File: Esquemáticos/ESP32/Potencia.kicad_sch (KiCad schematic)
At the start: 11 parts, among them J3 Barrel_Jack, SW1 SW_DIP_x01, U5 AMS1117-5.0, U6 AMS1117-3.3

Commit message: Eliminando el error de autosave
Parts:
- added D1: Led_ON, LED_SMD:LED_1206_3216Metric, symbol LED:IR26-21C_L110_TR8
- SW1: footprint (none) -> Button_Switch_SMD:SW_DIP_SPSTx01_Slide_6.7x4.1mm_W6.73mm_P2.54mm_LowProfile_JPin
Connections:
- net 3.3V: now also D1.2 (A)
- net GND: now also D1.1 (K)
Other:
- note added: "Led de encendido"
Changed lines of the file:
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@@
+    (stroke (width 0) (type default) (color 0 0 0 0))
+  )
+  (polyline (pts (xy 238.76 123.19) (xy 238.76 152.4))
     (stroke (width 0) (type default) (color 0 0 0 0))
   )
@@
     (stroke (width 0) (type default) (color 0 0 0 0))
   )
+  (polyline (pts (xy 257.81 152.4) (xy 257.81 123.19))
+    (stroke (width 0) (type default) (color 0 0 0 0))
+  )
   (wire (pts (xy 163.83 138.43) (xy 163.83 143.51))
     (stroke (width 0) (type default) (color 0 0 0 0))
@@
     (stroke (width 0) (type default) (color 0 0 0 0))
   )
+  (polyline (pts (xy 238.76 123.19) (xy 257.81 123.19))
+    (stroke (width 0) (type default) (color 0 0 0 0))
+  )
+  (wire (pts (xy 245.11 139.7) (xy 245.11 142.24))
+    (stroke (width 0) (type default) (color 0 0 0 0))
+  )
   (wire (pts (xy 207.01 91.44) (xy 207.01 88.9))
     (stroke (width 0) (type default) (color 0 0 0 0))
@@
     (stroke (width 0) (type default) (color 0 0 0 0))
   )
+  (wire (pts (xy 245.11 130.81) (xy 245.11 132.08))
+    (stroke (width 0) (type default) (color 0 0 0 0))
+  )
   (wire (pts (xy 163.83 120.65) (xy 163.83 128.27))
     (stroke (width 0) (type default) (color 0 0 0 0))
@@
     (stroke (width 0) (type default) (color 0 0 0 0))
   )
+  (polyline (pts (xy 238.76 152.4) (xy 257.81 152.4))
+    (stroke (width 0) (type default) (color 0 0 0 0))
+  )
   (wire (pts (xy 160.02 88.9) (xy 160.02 91.44))
     (stroke (width 0) (type default) (color 0 0 0 0))
@@
   )
   (text "Entrada de alimentación de 12V mediante un Jack " (at 76.2 123.19 0)
+    (effects (font (size 1.27 1.27)) (justify left bottom))
+  )
+  (text "Led de encendido\n" (at 238.76 156.21 0)
     (effects (font (size 1.27 1.27)) (justify left bottom))
   )
@@
   )
   (hierarchical_label "3.3V" (shape input) (at 207.01 123.19 90)
+    (effects (font (size 1.27 1.27)) (justify left))
+  )
+  (hierarchical_label "3.3V" (shape input) (at 245.11 130.81 90)
     (effects (font (size 1.27 1.27)) (justify left))
   )
@@
     (pin "1")
   )
+  (symbol (lib_id "LED:IR26-21C_L110_TR8") (at 245.11 135.89 90) (unit 1)
+    (in_bom yes) (on_board yes) (fields_autoplaced)
+    (property "Reference" "D1" (id 0) (at 248.92 136.2074 90)
+      (effects (font (size 1.27 1.27)) (justify right))
+    )
+    (property "Value" "Led_ON" (id 1) (at 248.92 138.7474 90)
+      (effects (font (size 1.27 1.27)) (justify right))
+    )
+    (property "Footprint" "LED_SMD:LED_1206_3216Metric" (id 2) (at 240.03 135.89 0)
+      (effects (font (size 1.27 1.27)) hide)
+    )
+    (property "Datasheet" "http://www.everlight.com/file/ProductFile/IR26-21C-L110-TR8.pdf" (id 3) (at 245.11 135.89 0)
+      (effects (font (size 1.27 1.27)) hide)
+    )
+    (pin "1")
+    (pin "2")
+  )
   (symbol (lib_id "Device:C_Polarized_US") (at 163.83 134.62 0) (unit 1)
     (in_bom yes) (on_board yes)
@@
     (pin "1")
   )
+  (symbol (lib_id "power:GND") (at 245.11 142.24 0) (unit 1)
+    (in_bom yes) (on_board yes) (fields_autoplaced)
+    (property "Reference" "#PWR0101" (id 0) (at 245.11 148.59 0)
+      (effects (font (size 1.27 1.27)) hide)
+    )
+    (property "Value" "GND" (id 1) (at 245.11 147.32 0))
+    (property "Footprint" "" (id 2) (at 245.11 142.24 0)
+      (effects (font (size 1.27 1.27)) hide)
+    )
+    (property "Datasheet" "" (id 3) (at 245.11 142.24 0)
+      (effects (font (size 1.27 1.27)) hide)
+    )
+    (pin "1")
+  )
   (symbol (lib_id "power:GND") (at 113.03 107.95 0) (unit 1)
     (in_bom yes) (on_board yes) (fields_autoplaced)
@@
     (property "Reference" "SW1" (id 0) (at 88.9 81.28 0))
     (property "Value" "SW_DIP_x01" (id 1) (at 88.9 83.82 0))
-    (property "Footprint" "" (id 2) (at 88.9 88.9 0)
-      (effects (font (size 1.27 1.27)) hide)
-    )
+    (property "Footprint" "Button_Switch_SMD:SW_DIP_SPSTx01_Slide_6.7x4.1mm_W6.73mm_P2.54mm_LowProfile_JPin" (id 2) (at 88.9 88.9 0)
+      (effects (font (size 1.27 1.27)) hide)
+    )

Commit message: Etiquetas globales para alimentación añadidas
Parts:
- C11: footprint (none) -> Capacitor_SMD:C_0201_0603Metric_Pad0.64x0.40mm_HandSolder
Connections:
- net Earth is gone; now on net GND: J3.2
- net 12V renamed +12V
- net 3.3V renamed +3.3V
- net 5V renamed +5V
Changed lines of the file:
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@@
     (effects (font (size 1.27 1.27)) (justify left bottom))
-  )
-  (hierarchical_label "3.3V" (shape input) (at 207.01 123.19 90)
-    (effects (font (size 1.27 1.27)) (justify left))
-  )
-  (hierarchical_label "3.3V" (shape input) (at 245.11 130.81 90)
-    (effects (font (size 1.27 1.27)) (justify left))
-  )
-  (hierarchical_label "12V" (shape input) (at 128.27 82.55 90)
-    (effects (font (size 1.27 1.27)) (justify left))
-  )
-  (hierarchical_label "5V" (shape input) (at 207.01 83.82 90)
-    (effects (font (size 1.27 1.27)) (justify left))
   )
   (symbol (lib_id "Regulator_Linear:AMS1117-5.0") (at 182.88 88.9 0) (unit 1)
@@
     (pin "1")
   )
+  (symbol (lib_id "power:+12V") (at 128.27 82.55 0) (unit 1)
+    (in_bom yes) (on_board yes) (fields_autoplaced)
+    (property "Reference" "#PWR021" (id 0) (at 128.27 86.36 0)
+      (effects (font (size 1.27 1.27)) hide)
+    )
+    (property "Value" "+12V" (id 1) (at 128.27 77.47 0))
+    (property "Footprint" "" (id 2) (at 128.27 82.55 0)
+      (effects (font (size 1.27 1.27)) hide)
+    )
+    (property "Datasheet" "" (id 3) (at 128.27 82.55 0)
+      (effects (font (size 1.27 1.27)) hide)
+    )
+    (pin "1")
+  )
   (symbol (lib_id "LED:IR26-21C_L110_TR8") (at 245.11 135.89 90) (unit 1)
     (in_bom yes) (on_board yes) (fields_autoplaced)
@@
     )
     (property "Datasheet" "" (id 3) (at 182.88 105.41 0)
+      (effects (font (size 1.27 1.27)) hide)
+    )
+    (pin "1")
+  )
+  (symbol (lib_id "power:GND") (at 78.74 107.95 0) (unit 1)
+    (in_bom yes) (on_board yes) (fields_autoplaced)
+    (property "Reference" "#PWR01" (id 0) (at 78.74 114.3 0)
+      (effects (font (size 1.27 1.27)) hide)
+    )
+    (property "Value" "GND" (id 1) (at 78.74 113.03 0))
+    (property "Footprint" "" (id 2) (at 78.74 107.95 0)
+      (effects (font (size 1.27 1.27)) hide)
+    )
+    (property "Datasheet" "" (id 3) (at 78.74 107.95 0)
       (effects (font (size 1.27 1.27)) hide)
     )
@@
     (pin "3")
   )
-  (symbol (lib_id "power:Earth") (at 78.74 107.95 0) (unit 1)
-    (in_bom yes) (on_board yes) (fields_autoplaced)
-    (property "Reference" "#PWR01" (id 0) (at 78.74 114.3 0)
-      (effects (font (size 1.27 1.27)) hide)
-    )
-    (property "Value" "Earth" (id 1) (at 78.74 111.76 0)
-      (effects (font (size 1.27 1.27)) hide)
-    )
-    (property "Footprint" "" (id 2) (at 78.74 107.95 0)
-      (effects (font (size 1.27 1.27)) hide)
-    )
-    (property "Datasheet" "~" (id 3) (at 78.74 107.95 0)
+  (symbol (lib_id "power:+5V") (at 207.01 83.82 0) (unit 1)
+    (in_bom yes) (on_board yes) (fields_autoplaced)
+    (property "Reference" "#PWR022" (id 0) (at 207.01 87.63 0)
+      (effects (font (size 1.27 1.27)) hide)
+    )
+    (property "Value" "+5V" (id 1) (at 207.01 78.74 0))
+    (property "Footprint" "" (id 2) (at 207.01 83.82 0)
+      (effects (font (size 1.27 1.27)) hide)
+    )
+    (property "Datasheet" "" (id 3) (at 207.01 83.82 0)
+      (effects (font (size 1.27 1.27)) hide)
+    )
+    (pin "1")
+  )
+  (symbol (lib_id "power:+3.3V") (at 207.01 123.19 0) (unit 1)
+    (in_bom yes) (on_board yes) (fields_autoplaced)
+    (property "Reference" "#PWR023" (id 0) (at 207.01 127 0)
+      (effects (font (size 1.27 1.27)) hide)
+    )
+    (property "Value" "+3.3V" (id 1) (at 207.01 118.11 0))
+    (property "Footprint" "" (id 2) (at 207.01 123.19 0)
+      (effects (font (size 1.27 1.27)) hide)
+    )
+    (property "Datasheet" "" (id 3) (at 207.01 123.19 0)
       (effects (font (size 1.27 1.27)) hide)
     )
@@
       (effects (font (size 1.27 1.27)) (justify left))
     )
-    (property "Footprint" "" (id 2) (at 128.27 97.79 0)
+    (property "Footprint" "Capacitor_SMD:C_0201_0603Metric_Pad0.64x0.40mm_HandSolder" (id 2) (at 128.27 97.79 0)
       (effects (font (size 1.27 1.27)) hide)
     )
@@
     (pin "2")
   )
+  (symbol (lib_id "power:+3.3V") (at 245.11 130.81 0) (unit 1)
+    (in_bom yes) (on_board yes) (fields_autoplaced)
+    (property "Reference" "#PWR024" (id 0) (at 245.11 134.62 0)
+      (effects (font (size 1.27 1.27)) hide)
+    )
+    (property "Value" "+3.3V" (id 1) (at 245.11 125.73 0))
+    (property "Footprint" "" (id 2) (at 245.11 130.81 0)
+      (effects (font (size 1.27 1.27)) hide)
+    )
+    (property "Datasheet" "" (id 3) (at 245.11 130.81 0)
+      (effects (font (size 1.27 1.27)) hide)
+    )
+    (pin "1")
+  )
   (symbol (lib_id "power:GND") (at 182.88 144.78 0) (unit 1)

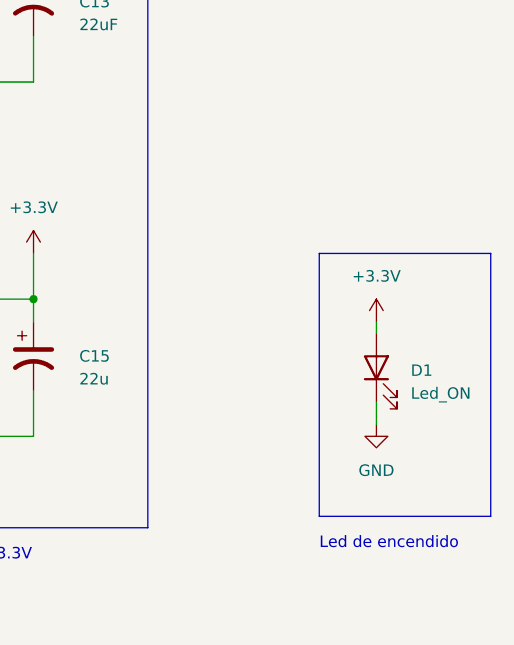
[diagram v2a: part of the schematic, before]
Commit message: añadí leds
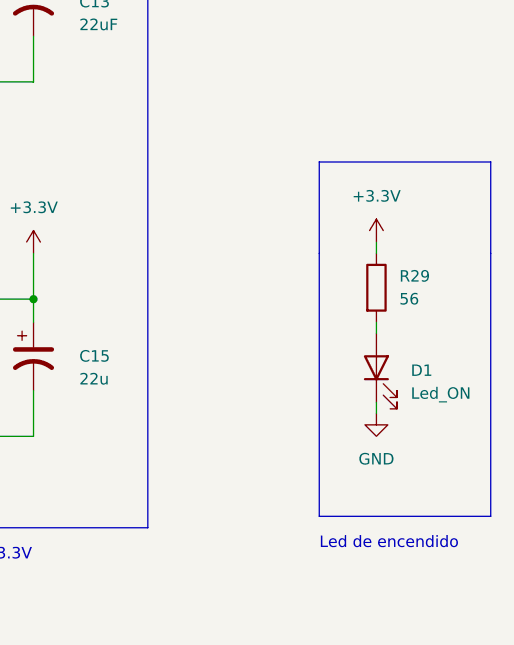
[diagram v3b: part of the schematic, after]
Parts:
- added R29: 56, Resistor_SMD:R_1206_3216Metric_Pad1.30x1.75mm_HandSolder, symbol Device:R
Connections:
- net +3.3V: now also R29.1; no longer D1.2 (A)
- new net: D1.2 (A), R29.2
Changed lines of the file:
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@@
+    (stroke (width 0) (type default) (color 0 0 0 0))
+  )
+  (wire (pts (xy 245.11 121.92) (xy 245.11 123.19))
     (stroke (width 0) (type default) (color 0 0 0 0))
   )
@@
     (stroke (width 0) (type default) (color 0 0 0 0))
   )
+  (wire (pts (xy 245.11 130.81) (xy 245.11 132.08))
+    (stroke (width 0) (type default) (color 0 0 0 0))
+  )
+  (polyline (pts (xy 238.76 123.19) (xy 238.76 113.03))
+    (stroke (width 0) (type default) (color 0 0 0 0))
+  )
   (polyline (pts (xy 257.81 152.4) (xy 257.81 123.19))
     (stroke (width 0) (type default) (color 0 0 0 0))
@@
     (stroke (width 0) (type default) (color 0 0 0 0))
   )
-  (polyline (pts (xy 238.76 123.19) (xy 257.81 123.19))
-    (stroke (width 0) (type default) (color 0 0 0 0))
-  )
-  (wire (pts (xy 245.11 139.7) (xy 245.11 142.24))
+  (wire (pts (xy 245.11 139.7) (xy 245.11 140.97))
     (stroke (width 0) (type default) (color 0 0 0 0))
   )
@@
     (stroke (width 0) (type default) (color 0 0 0 0))
   )
-  (wire (pts (xy 245.11 130.81) (xy 245.11 132.08))
-    (stroke (width 0) (type default) (color 0 0 0 0))
-  )
   (wire (pts (xy 163.83 120.65) (xy 163.83 128.27))
     (stroke (width 0) (type default) (color 0 0 0 0))
@@
     (stroke (width 0) (type default) (color 0 0 0 0))
   )
+  (polyline (pts (xy 238.76 113.03) (xy 257.81 113.03))
+    (stroke (width 0) (type default) (color 0 0 0 0))
+  )
   (wire (pts (xy 182.88 143.51) (xy 182.88 144.78))
     (stroke (width 0) (type default) (color 0 0 0 0))
@@
   )
   (wire (pts (xy 160.02 88.9) (xy 160.02 91.44))
+    (stroke (width 0) (type default) (color 0 0 0 0))
+  )
+  (polyline (pts (xy 257.81 113.03) (xy 257.81 123.19))
     (stroke (width 0) (type default) (color 0 0 0 0))
   )
@@
     (pin "2")
   )
-  (symbol (lib_id "power:+3.3V") (at 245.11 130.81 0) (unit 1)
-    (in_bom yes) (on_board yes) (fields_autoplaced)
-    (property "Reference" "#PWR024" (id 0) (at 245.11 134.62 0)
-      (effects (font (size 1.27 1.27)) hide)
-    )
-    (property "Value" "+3.3V" (id 1) (at 245.11 125.73 0))
-    (property "Footprint" "" (id 2) (at 245.11 130.81 0)
-      (effects (font (size 1.27 1.27)) hide)
-    )
-    (property "Datasheet" "" (id 3) (at 245.11 130.81 0)
+  (symbol (lib_id "power:+3.3V") (at 245.11 121.92 0) (unit 1)
+    (in_bom yes) (on_board yes) (fields_autoplaced)
+    (property "Reference" "#PWR024" (id 0) (at 245.11 125.73 0)
+      (effects (font (size 1.27 1.27)) hide)
+    )
+    (property "Value" "+3.3V" (id 1) (at 245.11 116.84 0))
+    (property "Footprint" "" (id 2) (at 245.11 121.92 0)
+      (effects (font (size 1.27 1.27)) hide)
+    )
+    (property "Datasheet" "" (id 3) (at 245.11 121.92 0)
       (effects (font (size 1.27 1.27)) hide)
     )
@@
     (pin "1")
   )
-  (symbol (lib_id "power:GND") (at 245.11 142.24 0) (unit 1)
-    (in_bom yes) (on_board yes) (fields_autoplaced)
-    (property "Reference" "#PWR0101" (id 0) (at 245.11 148.59 0)
-      (effects (font (size 1.27 1.27)) hide)
-    )
-    (property "Value" "GND" (id 1) (at 245.11 147.32 0))
-    (property "Footprint" "" (id 2) (at 245.11 142.24 0)
-      (effects (font (size 1.27 1.27)) hide)
-    )
-    (property "Datasheet" "" (id 3) (at 245.11 142.24 0)
-      (effects (font (size 1.27 1.27)) hide)
-    )
-    (pin "1")
+  (symbol (lib_id "power:GND") (at 245.11 140.97 0) (unit 1)
+    (in_bom yes) (on_board yes) (fields_autoplaced)
+    (property "Reference" "#PWR0101" (id 0) (at 245.11 147.32 0)
+      (effects (font (size 1.27 1.27)) hide)
+    )
+    (property "Value" "GND" (id 1) (at 245.11 146.05 0))
+    (property "Footprint" "" (id 2) (at 245.11 140.97 0)
+      (effects (font (size 1.27 1.27)) hide)
+    )
+    (property "Datasheet" "" (id 3) (at 245.11 140.97 0)
+      (effects (font (size 1.27 1.27)) hide)
+    )
+    (pin "1")
+  )
+  (symbol (lib_id "Device:R") (at 245.11 127 0) (unit 1)
+    (in_bom yes) (on_board yes) (fields_autoplaced)
+    (property "Reference" "R29" (id 0) (at 247.65 125.7299 0)
+      (effects (font (size 1.27 1.27)) (justify left))
+    )
+    (property "Value" "56" (id 1) (at 247.65 128.2699 0)
+      (effects (font (size 1.27 1.27)) (justify left))
+    )
+    (property "Footprint" "Resistor_SMD:R_1206_3216Metric_Pad1.30x1.75mm_HandSolder" (id 2) (at 243.332 127 90)
+      (effects (font (size 1.27 1.27)) hide)
+    )
+    (property "Datasheet" "~" (id 3) (at 245.11 127 0)
+      (effects (font (size 1.27 1.27)) hide)
+    )
+    (pin "1")
+    (pin "2")
   )
   (symbol (lib_id "power:GND") (at 113.03 107.95 0) (unit 1)

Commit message: Potencia - Final
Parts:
- removed C10: 100nF, Capacitor_SMD:C_0603_1608Metric_Pad1.08x0.95mm_HandSolder, symbol Device:C
- C11: value 1000uF -> 22uF; footprint Capacitor_SMD:C_0201_0603Metric_Pad0.64x0.40mm_HandSolder -> Capacitor_SMD:C_0603_1608Metric_Pad1.08x0.95mm_HandSolder
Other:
- note added: "Contiene un filtro de condensador para eliminar cualquier tipo de rizado"
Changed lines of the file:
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@@
 (kicad_sch (version 20211123) (generator eeschema)
   (paper "A4")
-  (junction (at 113.03 88.9) (diameter 0) (color 0 0 0 0)
-  )
   (junction (at 160.02 88.9) (diameter 0) (color 0 0 0 0)
   )
@@
     (stroke (width 0) (type default) (color 0 0 0 0))
   )
-  (wire (pts (xy 113.03 88.9) (xy 113.03 93.98))
-    (stroke (width 0) (type default) (color 0 0 0 0))
-  )
   (wire (pts (xy 163.83 128.27) (xy 163.83 130.81))
     (stroke (width 0) (type default) (color 0 0 0 0))
@@
     (stroke (width 0) (type default) (color 0 0 0 0))
   )
-  (wire (pts (xy 113.03 101.6) (xy 113.03 107.95))
-    (stroke (width 0) (type default) (color 0 0 0 0))
-  )
   (wire (pts (xy 182.88 104.14) (xy 182.88 105.41))
     (stroke (width 0) (type default) (color 0 0 0 0))
@@
   )
   (text "Led de encendido\n" (at 238.76 156.21 0)
+    (effects (font (size 1.27 1.27)) (justify left bottom))
+  )
+  (text "Contiene un filtro de condensador para eliminar cualquier tipo de rizado\n"
+    (at 68.58 127 0)
     (effects (font (size 1.27 1.27)) (justify left bottom))
   )
@@
     (pin "2")
   )
-  (symbol (lib_id "Device:C") (at 113.03 97.79 0) (unit 1)
-    (in_bom yes) (on_board yes) (fields_autoplaced)
-    (property "Reference" "C10" (id 0) (at 116.84 96.5199 0)
-      (effects (font (size 1.27 1.27)) (justify left))
-    )
-    (property "Value" "100nF" (id 1) (at 116.84 99.0599 0)
-      (effects (font (size 1.27 1.27)) (justify left))
-    )
-    (property "Footprint" "Capacitor_SMD:C_0603_1608Metric_Pad1.08x0.95mm_HandSolder" (id 2) (at 113.9952 101.6 0)
-      (effects (font (size 1.27 1.27)) hide)
-    )
-    (property "Datasheet" "~" (id 3) (at 113.03 97.79 0)
-      (effects (font (size 1.27 1.27)) hide)
-    )
-    (pin "1")
-    (pin "2")
-  )
   (symbol (lib_id "power:GND") (at 182.88 105.41 0) (unit 1)
     (in_bom yes) (on_board yes) (fields_autoplaced)
@@
       (effects (font (size 1.27 1.27)) (justify left))
     )
-    (property "Value" "1000uF" (id 1) (at 132.08 98.4249 0)
-      (effects (font (size 1.27 1.27)) (justify left))
-    )
-    (property "Footprint" "Capacitor_SMD:C_0201_0603Metric_Pad0.64x0.40mm_HandSolder" (id 2) (at 128.27 97.79 0)
+    (property "Value" "22uF" (id 1) (at 132.08 98.4249 0)
+      (effects (font (size 1.27 1.27)) (justify left))
+    )
+    (property "Footprint" "Capacitor_SMD:C_0603_1608Metric_Pad1.08x0.95mm_HandSolder" (id 2) (at 128.27 97.79 0)
       (effects (font (size 1.27 1.27)) hide)
     )
@@
     (pin "2")
   )
-  (symbol (lib_id "power:GND") (at 113.03 107.95 0) (unit 1)
-    (in_bom yes) (on_board yes) (fields_autoplaced)
-    (property "Reference" "#PWR02" (id 0) (at 113.03 114.3 0)
-      (effects (font (size 1.27 1.27)) hide)
-    )
-    (property "Value" "GND" (id 1) (at 113.03 113.03 0))
-    (property "Footprint" "" (id 2) (at 113.03 107.95 0)
-      (effects (font (size 1.27 1.27)) hide)
-    )
-    (property "Datasheet" "" (id 3) (at 113.03 107.95 0)
-      (effects (font (size 1.27 1.27)) hide)
-    )
-    (pin "1")
-  )
   (symbol (lib_id "Switch:SW_DIP_x01") (at 88.9 88.9 0) (unit 1)

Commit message: Actualizadas las huellas de R y C
De acuerdo con la recomendación del profe, ahora todas son 0603.
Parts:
- C12: footprint Capacitor_SMD:C_1206_3216Metric_Pad1.33x1.80mm_HandSolder -> Capacitor_SMD:C_0603_1608Metric_Pad1.08x0.95mm_HandSolder
- D1: footprint LED_SMD:LED_1206_3216Metric -> LED_SMD:LED_0603_1608Metric_Pad1.05x0.95mm_HandSolder
- R29: footprint Resistor_SMD:R_1206_3216Metric_Pad1.30x1.75mm_HandSolder -> Resistor_SMD:R_0603_1608Metric_Pad0.98x0.95mm_HandSolder
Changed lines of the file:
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@@
       (effects (font (size 1.27 1.27)) (justify left))
     )
-    (property "Footprint" "Capacitor_SMD:C_1206_3216Metric_Pad1.33x1.80mm_HandSolder" (id 2) (at 160.02 95.25 0)
+    (property "Footprint" "Capacitor_SMD:C_0603_1608Metric_Pad1.08x0.95mm_HandSolder" (id 2) (at 160.02 95.25 0)
       (effects (font (size 1.27 1.27)) hide)
     )
@@
       (effects (font (size 1.27 1.27)) (justify right))
     )
-    (property "Footprint" "LED_SMD:LED_1206_3216Metric" (id 2) (at 240.03 135.89 0)
+    (property "Footprint" "LED_SMD:LED_0603_1608Metric_Pad1.05x0.95mm_HandSolder" (id 2) (at 240.03 135.89 0)
       (effects (font (size 1.27 1.27)) hide)
     )
@@
       (effects (font (size 1.27 1.27)) (justify left))
     )
-    (property "Footprint" "Resistor_SMD:R_1206_3216Metric_Pad1.30x1.75mm_HandSolder" (id 2) (at 243.332 127 90)
-      (effects (font (size 1.27 1.27)) hide)
-    )
+    (property "Footprint" "Resistor_SMD:R_0603_1608Metric_Pad0.98x0.95mm_HandSolder" (id 2) (at 243.332 127 90)
+      (effects (font (size 1.27 1.27)) hide)
+    )

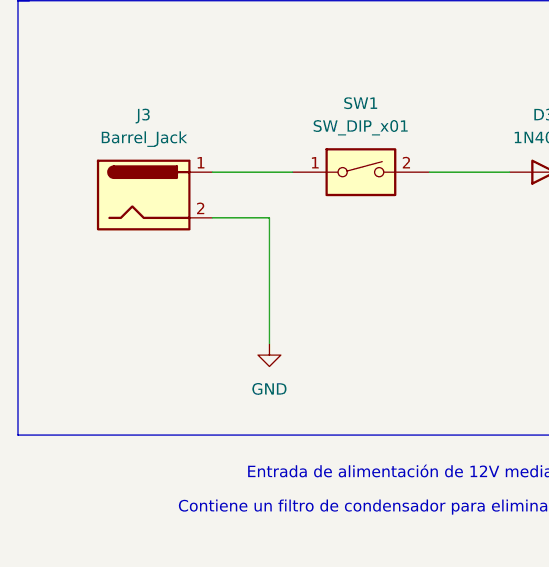
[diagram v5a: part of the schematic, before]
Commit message: PCB versión 1 (Faltan zonas de GND)
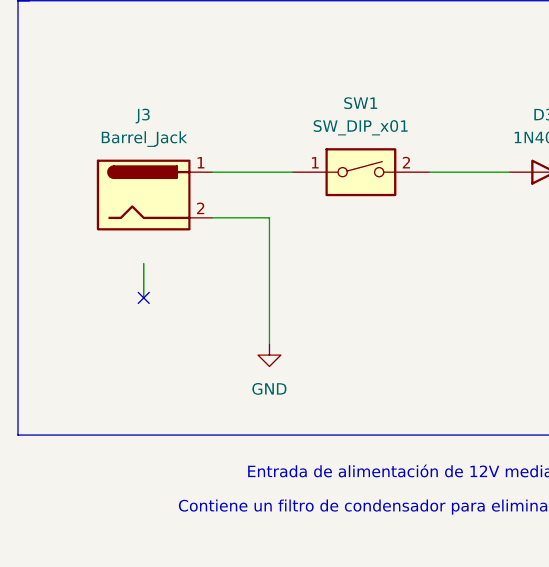
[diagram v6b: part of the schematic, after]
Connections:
- no-connect marks 0 -> 1
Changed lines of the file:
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@@
   (junction (at 182.88 104.14) (diameter 0) (color 0 0 0 0)
   )
+  (no_connect (at 64.77 102.87))
   (wire (pts (xy 182.88 104.14) (xy 207.01 104.14))
     (stroke (width 0) (type default) (color 0 0 0 0))
@@
     (stroke (width 0) (type default) (color 0 0 0 0))
   )
+  (wire (pts (xy 64.77 102.87) (xy 64.77 99.06))
+    (stroke (width 0) (type default) (color 0 0 0 0))
+  )
